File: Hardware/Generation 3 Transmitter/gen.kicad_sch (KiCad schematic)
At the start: 21 parts, among them SW1 POWER, SW2 INVERT, U1 LEFT STICK, U2 RIGHT STICK, U3 ADS7830, U4 DISPLAY, U5 XIAO, U6 NRF24L01_Breakout

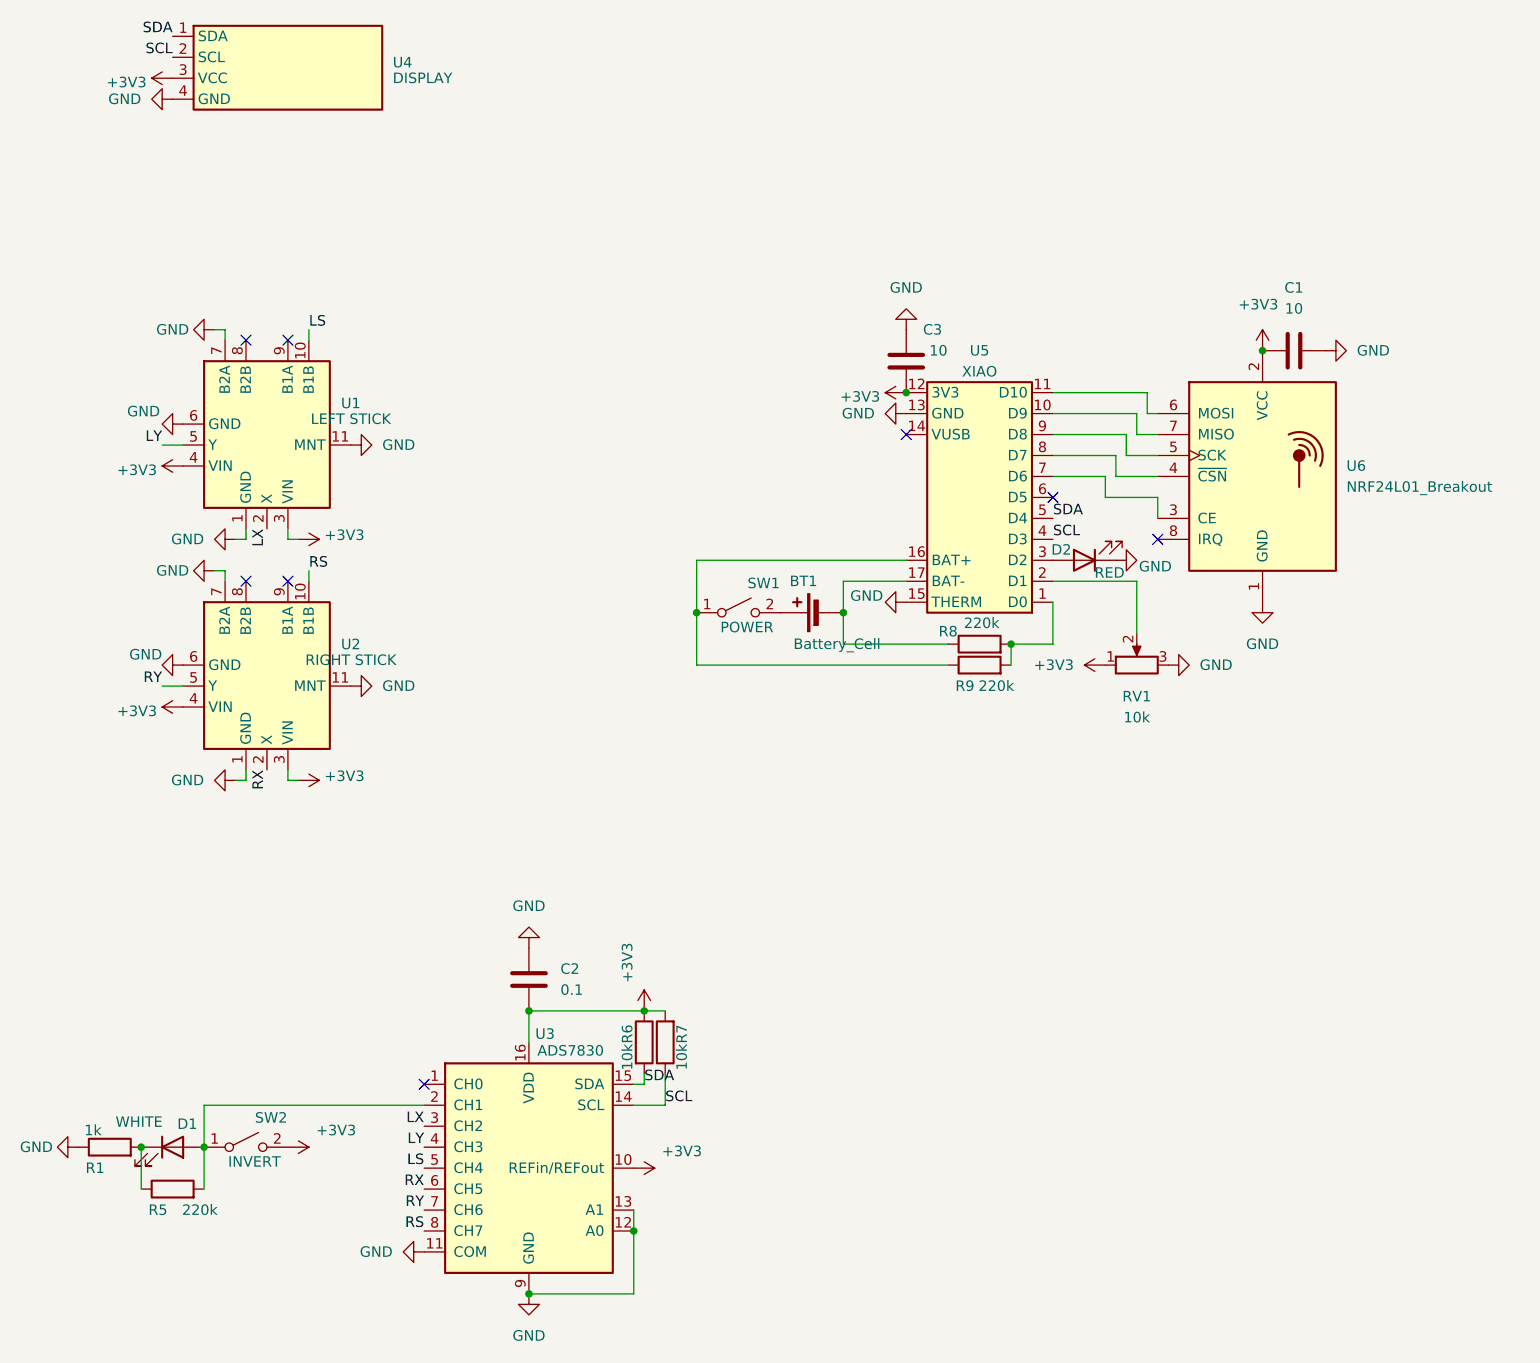
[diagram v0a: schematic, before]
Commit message: Redoing the SDMD Kllip in an intelligent way, changing some receiver things, and designing a transmitter board
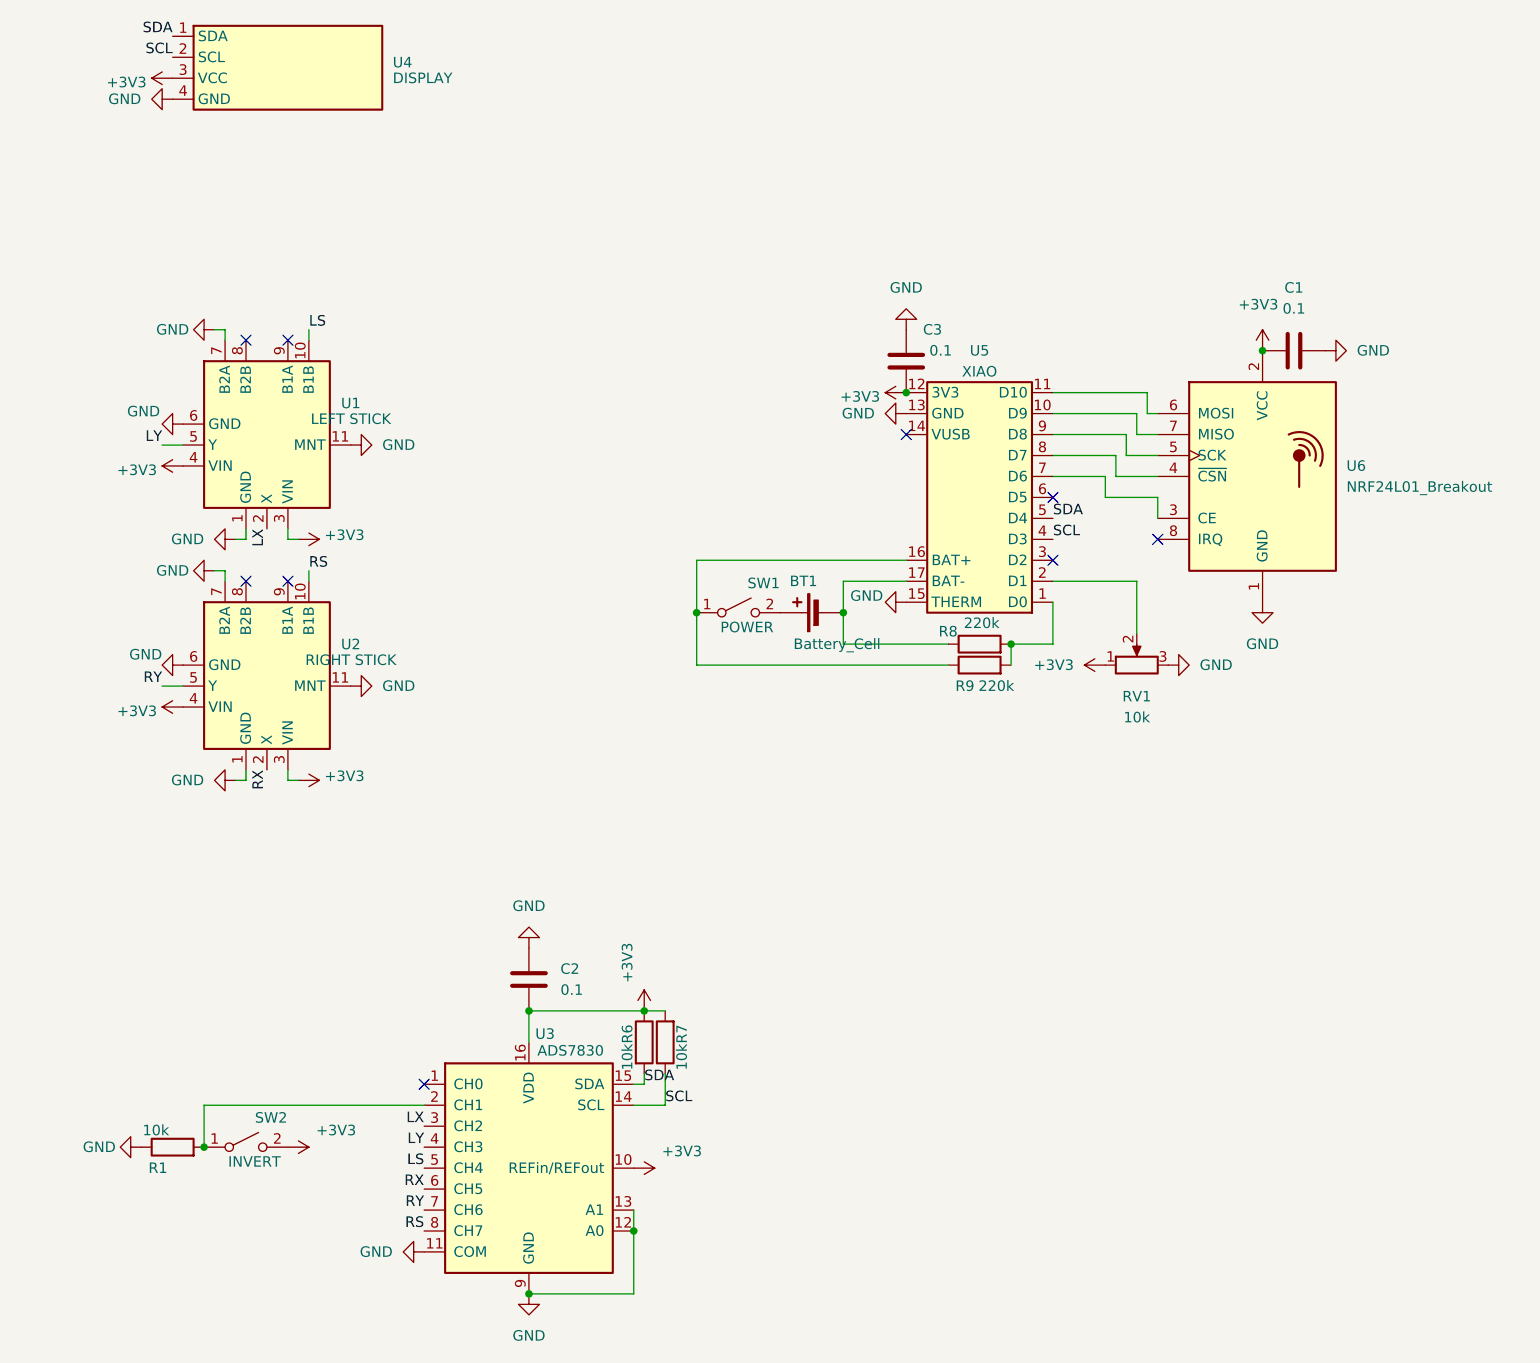
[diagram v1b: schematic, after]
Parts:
- removed D1: WHITE, Connector_PinHeader_2.54mm:PinHeader_1x02_P2.54mm_Vertical, symbol Device:LED
- removed D2: RED, Connector_PinHeader_2.54mm:PinHeader_1x02_P2.54mm_Vertical, symbol Device:LED
- removed R5: 220k, Resistor_SMD:R_0805_2012Metric, symbol Device:R
- C1, C3: value 10 -> 0.1
- R1: value 1k -> 10k
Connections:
- net at R1.2: now also SW2.1 (A), U3.2 (CH1)
- no-connect marks 8 -> 9
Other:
- moved on the sheet: R1
